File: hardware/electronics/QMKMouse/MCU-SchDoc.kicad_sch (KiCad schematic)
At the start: 14 parts

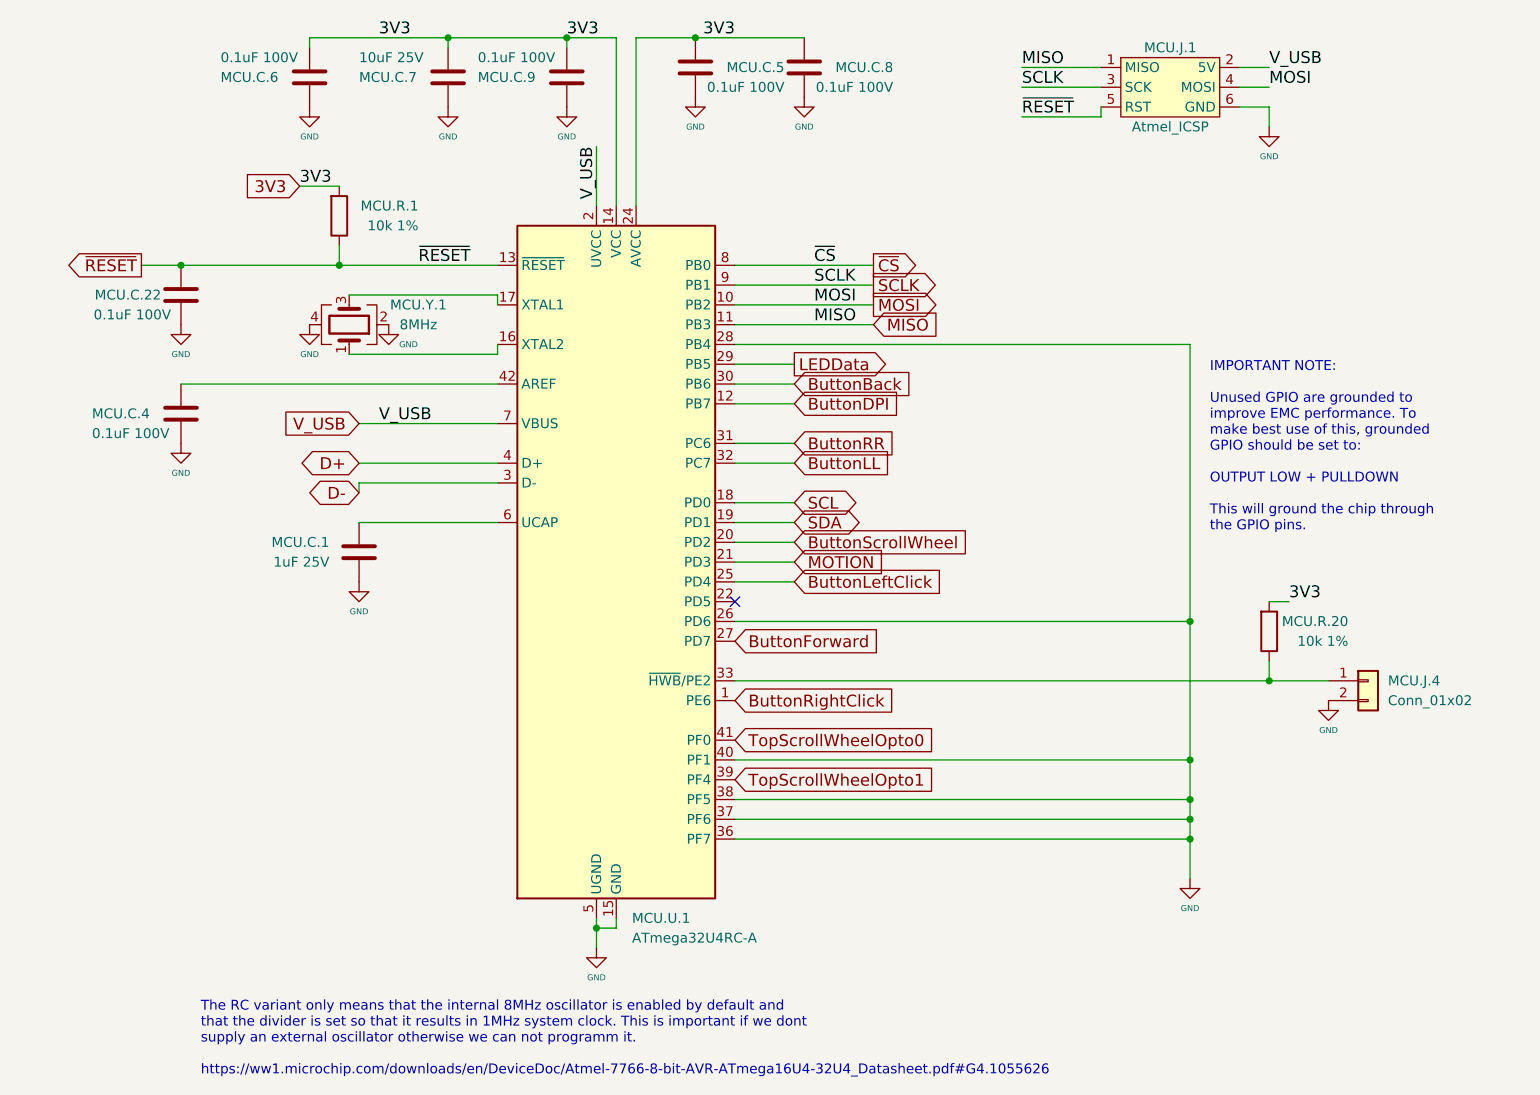
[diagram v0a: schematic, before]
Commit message: fix ERC errors and use hierarchy labels
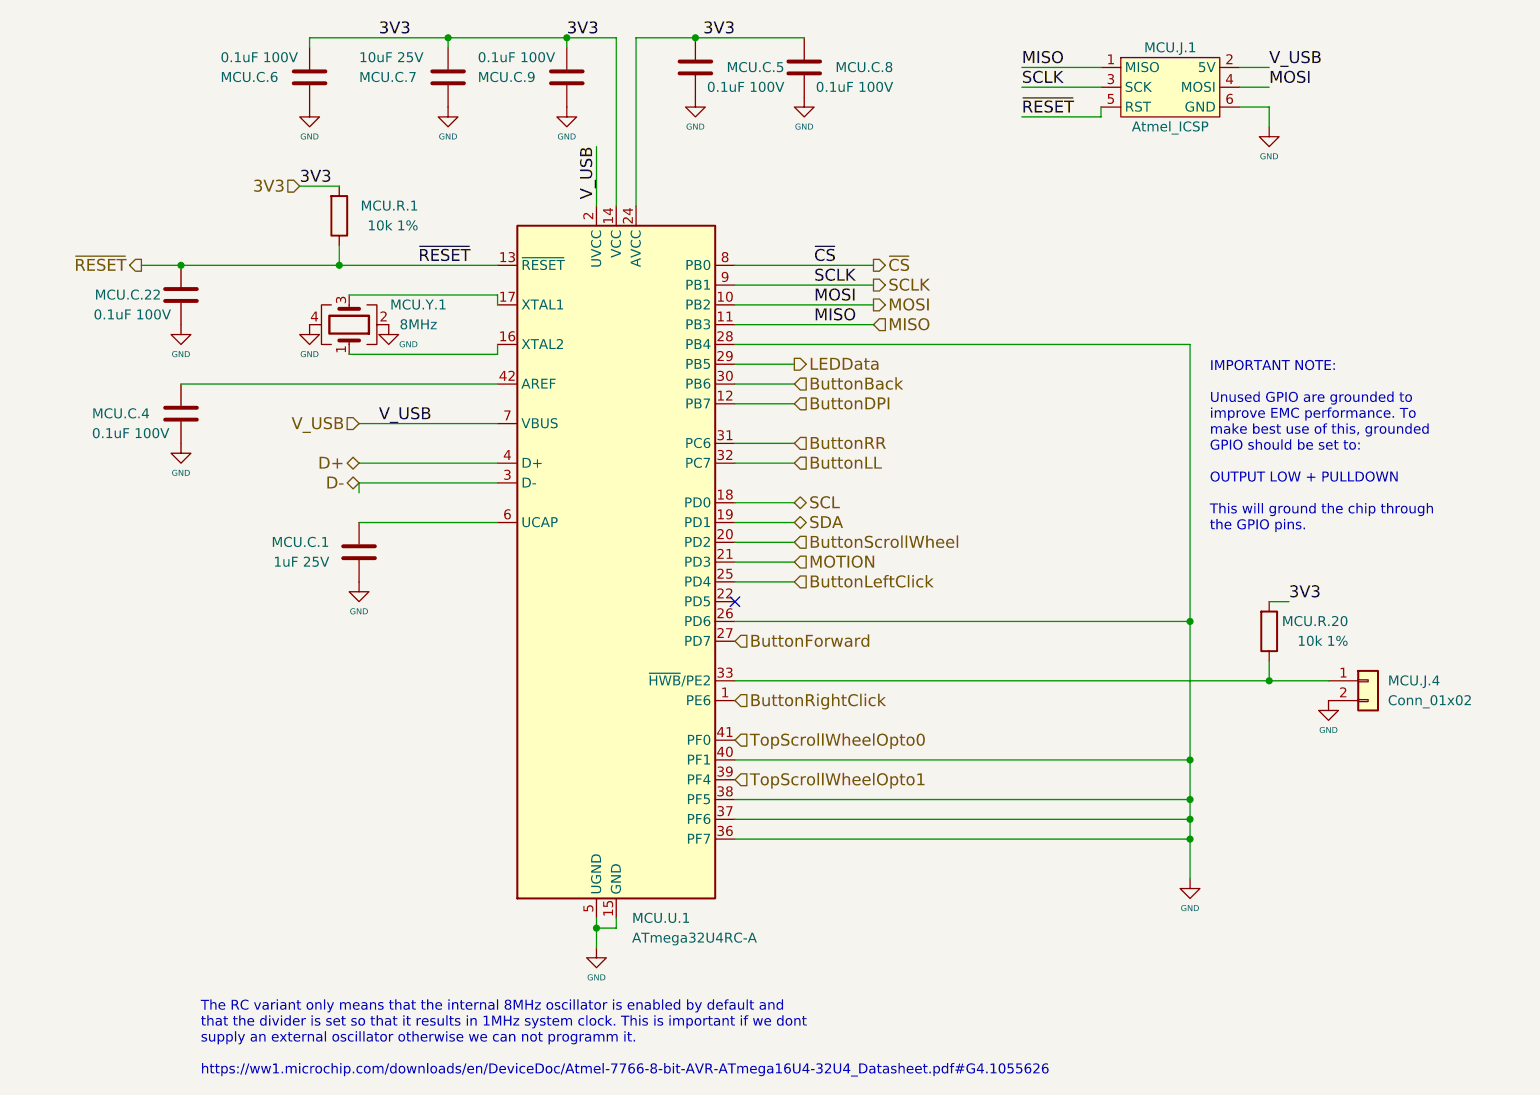
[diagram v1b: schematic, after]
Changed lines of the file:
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@@
     (effects (font (size 1.524 1.524)) (justify left bottom))
   )
-  (global_label "ButtonLeftClick" (shape input) (at 128.27 107.95 0) (fields_autoplaced)
+  (hierarchical_label "V_USB" (shape input) (at 72.39 87.63 180)
+    (effects (font (size 1.524 1.524)) (justify right))
+  )
+  (hierarchical_label "MOTION" (shape input) (at 128.27 105.41 0)
     (effects (font (size 1.524 1.524)) (justify left))
-    (property "Intersheet References" "${INTERSHEET_REFS}" (id 0) (at -90.17 -52.07 0)
-      (effects (font (size 1.27 1.27)) hide)
-    )
   )
-  (global_label "ButtonBack" (shape input) (at 128.27 82.55 0) (fields_autoplaced)
+  (hierarchical_label "~{CS}" (shape output) (at 138.43 67.31 0)
     (effects (font (size 1.524 1.524)) (justify left))
-    (property "Intersheet References" "${INTERSHEET_REFS}" (id 0) (at -90.17 -49.53 0)
-      (effects (font (size 1.27 1.27)) hide)
-    )
   )
-  (global_label "D+" (shape bidirectional) (at 72.39 92.71 180) (fields_autoplaced)
+  (hierarchical_label "MOSI" (shape output) (at 138.43 72.39 0)
+    (effects (font (size 1.524 1.524)) (justify left))
+  )
+  (hierarchical_label "ButtonRightClick" (shape input) (at 120.65 123.19 0)
+    (effects (font (size 1.524 1.524)) (justify left))
+  )
+  (hierarchical_label "SCL" (shape bidirectional) (at 128.27 97.79 0)
+    (effects (font (size 1.524 1.524)) (justify left))
+  )
+  (hierarchical_label "TopScrollWheelOpto0" (shape input) (at 120.65 128.27 0)
+    (effects (font (size 1.524 1.524)) (justify left))
+  )
+  (hierarchical_label "ButtonLL" (shape input) (at 128.27 92.71 0)
+    (effects (font (size 1.524 1.524)) (justify left))
+  )
+  (hierarchical_label "ButtonLeftClick" (shape input) (at 128.27 107.95 0)
+    (effects (font (size 1.524 1.524)) (justify left))
+  )
+  (hierarchical_label "3V3" (shape input) (at 64.77 57.15 180)
     (effects (font (size 1.524 1.524)) (justify right))
-    (property "Intersheet References" "${INTERSHEET_REFS}" (id 0) (at 166.37 217.17 0)
-      (effects (font (size 1.27 1.27)) (justify left) hide)
-    )
   )
-  (global_label "D-" (shape bidirectional) (at 72.39 96.52 180) (fields_autoplaced)
+  (hierarchical_label "ButtonRR" (shape input) (at 128.27 90.17 0)
+    (effects (font (size 1.524 1.524)) (justify left))
+  )
+  (hierarchical_label "ButtonForward" (shape input) (at 120.65 115.57 0)
+    (effects (font (size 1.524 1.524)) (justify left))
+  )
+  (hierarchical_label "ButtonBack" (shape input) (at 128.27 82.55 0)
+    (effects (font (size 1.524 1.524)) (justify left))
+  )
+  (hierarchical_label "SCLK" (shape output) (at 138.43 69.85 0)
+    (effects (font (size 1.524 1.524)) (justify left))
+  )
+  (hierarchical_label "ButtonDPI" (shape input) (at 128.27 85.09 0)
+    (effects (font (size 1.524 1.524)) (justify left))
+  )
+  (hierarchical_label "LEDData" (shape output) (at 128.27 80.01 0)
+    (effects (font (size 1.524 1.524)) (justify left))
+  )
+  (hierarchical_label "~{RESET}" (shape output) (at 44.45 67.31 180)
     (effects (font (size 1.524 1.524)) (justify right))
-    (property "Intersheet References" "${INTERSHEET_REFS}" (id 0) (at 166.37 215.9 0)
-      (effects (font (size 1.27 1.27)) (justify left) hide)
-    )
   )
-  (global_label "TopScrollWheelOpto1" (shape input) (at 120.65 133.35 0) (fields_autoplaced)
+  (hierarchical_label "TopScrollWheelOpto1" (shape input) (at 120.65 133.35 0)
     (effects (font (size 1.524 1.524)) (justify left))
-    (property "Intersheet References" "${INTERSHEET_REFS}" (id 0) (at -97.79 -52.07 0)
-      (effects (font (size 1.27 1.27)) hide)
-    )
   )
-  (global_label "~{CS}" (shape output) (at 138.43 67.31 0) (fields_autoplaced)
+  (hierarchical_label "D+" (shape bidirectional) (at 72.39 92.71 180)
+    (effects (font (size 1.524 1.524)) (justify right))
+  )
+  (hierarchical_label "MISO" (shape input) (at 138.43 74.93 0)
     (effects (font (size 1.524 1.524)) (justify left))
-    (property "Intersheet References" "${INTERSHEET_REFS}" (id 0) (at -97.79 -46.99 0)
-      (effects (font (size 1.27 1.27)) hide)
-    )
   )
-  (global_label "3V3" (shape input) (at 64.77 57.15 180) (fields_autoplaced)
+  (hierarchical_label "SDA" (shape bidirectional) (at 128.27 100.33 0)
+    (effects (font (size 1.524 1.524)) (justify left))
+  )
+  (hierarchical_label "ButtonScrollWheel" (shape input) (at 128.27 102.87 0)
+    (effects (font (size 1.524 1.524)) (justify left))
+  )
+  (hierarchical_label "D-" (shape bidirectional) (at 72.39 95.25 180)
     (effects (font (size 1.524 1.524)) (justify right))
-    (property "Intersheet References" "${INTERSHEET_REFS}" (id 0) (at 153.67 -97.79 0)
-      (effects (font (size 1.27 1.27)) (justify left) hide)
-    )
-  )
-  (global_label "ButtonRR" (shape input) (at 128.27 90.17 0) (fields_autoplaced)
-    (effects (font (size 1.524 1.524)) (justify left))
-    (property "Intersheet References" "${INTERSHEET_REFS}" (id 0) (at -90.17 -49.53 0)
-      (effects (font (size 1.27 1.27)) hide)
-    )
-  )
-  (global_label "ButtonScrollWheel" (shape input) (at 128.27 102.87 0) (fields_autoplaced)
-    (effects (font (size 1.524 1.524)) (justify left))
-    (property "Intersheet References" "${INTERSHEET_REFS}" (id 0) (at -90.17 -49.53 0)
-      (effects (font (size 1.27 1.27)) hide)
-    )
-  )
-  (global_label "TopScrollWheelOpto0" (shape input) (at 120.65 128.27 0) (fields_autoplaced)
-    (effects (font (size 1.524 1.524)) (justify left))
-    (property "Intersheet References" "${INTERSHEET_REFS}" (id 0) (at -97.79 -52.07 0)
-      (effects (font (size 1.27 1.27)) hide)
-    )
-  )
-  (global_label "ButtonRightClick" (shape input) (at 120.65 123.19 0) (fields_autoplaced)
-    (effects (font (size 1.524 1.524)) (justify left))
-    (property "Intersheet References" "${INTERSHEET_REFS}" (id 0) (at -97.79 -52.07 0)
-      (effects (font (size 1.27 1.27)) hide)
-    )
-  )
-  (global_label "LEDData" (shape output) (at 128.27 80.01 0) (fields_autoplaced)
-    (effects (font (size 1.524 1.524)) (justify left))
-    (property "Intersheet References" "${INTERSHEET_REFS}" (id 0) (at -90.17 -49.53 0)
-      (effects (font (size 1.27 1.27)) hide)
-    )
-  )
-  (global_label "MISO" (shape input) (at 138.43 74.93 0) (fields_autoplaced)
-    (effects (font (size 1.524 1.524)) (justify left))
-    (property "Intersheet References" "${INTERSHEET_REFS}" (id 0) (at -97.79 -46.99 0)
-      (effects (font (size 1.27 1.27)) hide)
-    )
-  )
-  (global_label "ButtonLL" (shape input) (at 128.27 92.71 0) (fields_autoplaced)
-    (effects (font (size 1.524 1.524)) (justify left))
-    (property "Intersheet References" "${INTERSHEET_REFS}" (id 0) (at -90.17 -49.53 0)
-      (effects (font (size 1.27 1.27)) hide)
-    )
-  )
-  (global_label "SCLK" (shape output) (at 138.43 69.85 0) (fields_autoplaced)
-    (effects (font (size 1.524 1.524)) (justify left))
-    (property "Intersheet References" "${INTERSHEET_REFS}" (id 0) (at -97.79 -46.99 0)
-      (effects (font (size 1.27 1.27)) hide)
-    )
-  )
-  (global_label "MOTION" (shape input) (at 128.27 105.41 0) (fields_autoplaced)
-    (effects (font (size 1.524 1.524)) (justify left))
-    (property "Intersheet References" "${INTERSHEET_REFS}" (id 0) (at -90.17 -49.53 0)
-      (effects (font (size 1.27 1.27)) hide)
-    )
-  )
-  (global_label "~{RESET}" (shape output) (at 44.45 67.31 180) (fields_autoplaced)
-    (effects (font (size 1.524 1.524)) (justify right))
-    (property "Intersheet References" "${INTERSHEET_REFS}" (id 0) (at 77.47 -97.79 0)
-      (effects (font (size 1.27 1.27)) (justify left) hide)
-    )
-  )
-  (global_label "MOSI" (shape output) (at 138.43 72.39 0) (fields_autoplaced)
-    (effects (font (size 1.524 1.524)) (justify left))
-    (property "Intersheet References" "${INTERSHEET_REFS}" (id 0) (at -97.79 -46.99 0)
-      (effects (font (size 1.27 1.27)) hide)
-    )
-  )
-  (global_label "V_USB" (shape input) (at 72.39 87.63 180) (fields_autoplaced)
-    (effects (font (size 1.524 1.524)) (justify right))
-    (property "Intersheet References" "${INTERSHEET_REFS}" (id 0) (at 166.37 -57.15 0)
-      (effects (font (size 1.27 1.27)) (justify left) hide)
-    )
-  )
-  (global_label "SDA" (shape bidirectional) (at 128.27 100.33 0) (fields_autoplaced)
-    (effects (font (size 1.524 1.524)) (justify left))
-    (property "Intersheet References" "${INTERSHEET_REFS}" (id 0) (at -90.17 -49.53 0)
-      (effects (font (size 1.27 1.27)) hide)
-    )
-  )
-  (global_label "SCL" (shape bidirectional) (at 128.27 97.79 0) (fields_autoplaced)
-    (effects (font (size 1.524 1.524)) (justify left))
-    (property "Intersheet References" "${INTERSHEET_REFS}" (id 0) (at -90.17 -49.53 0)
-      (effects (font (size 1.27 1.27)) hide)
-    )
-  )
-  (global_label "ButtonDPI" (shape input) (at 128.27 85.09 0) (fields_autoplaced)
-    (effects (font (size 1.524 1.524)) (justify left))
-    (property "Intersheet References" "${INTERSHEET_REFS}" (id 0) (at -90.17 -49.53 0)
-      (effects (font (size 1.27 1.27)) hide)
-    )
-  )
-  (global_label "ButtonForward" (shape input) (at 120.65 115.57 0) (fields_autoplaced)
-    (effects (font (size 1.524 1.524)) (justify left))
-    (property "Intersheet References" "${INTERSHEET_REFS}" (id 0) (at -97.79 -52.07 0)
-      (effects (font (size 1.27 1.27)) hide)
-    )
   )
   (symbol (lib_id "power:GND") (at 196.85 123.19 0) (unit 1)

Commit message: reference 3d model to all components
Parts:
- MCU.C.1, MCU.C.22, MCU.C.4, MCU.C.5, MCU.C.6, MCU.C.7, MCU.C.8, MCU.C.9: footprint Chip_Passives.PcbLib:0805 -> mouse_part:C_0805
- MCU.R.1, MCU.R.20: footprint Chip_Passives.PcbLib:0805 -> mouse_part:0805
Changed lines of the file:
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@@
       (effects (font (size 1.27 1.27)) (justify right))
     )
-    (property "Footprint" "Chip_Passives.PcbLib:0805" (id 2) (at 50.4952 67.31 0)
+    (property "Footprint" "mouse_part:C_0805" (id 2) (at 50.4952 67.31 0)
       (effects (font (size 1.27 1.27)) hide)
     )
@@
       (effects (font (size 1.27 1.27)) (justify left))
     )
-    (property "Footprint" "Chip_Passives.PcbLib:0805" (id 2) (at 50.4952 82.55 0)
+    (property "Footprint" "mouse_part:C_0805" (id 2) (at 50.4952 82.55 0)
       (effects (font (size 1.27 1.27)) hide)
     )
@@
       (effects (font (size 1.27 1.27)) (justify left))
     )
-    (property "Footprint" "Chip_Passives.PcbLib:0805" (id 2) (at 114.6048 38.1 0)
+    (property "Footprint" "mouse_part:C_0805" (id 2) (at 114.6048 38.1 0)
       (effects (font (size 1.27 1.27)) hide)
     )
@@
       (effects (font (size 1.27 1.27)) (justify left))
     )
-    (property "Footprint" "Chip_Passives.PcbLib:0805" (id 2) (at 100.0252 39.37 0)
+    (property "Footprint" "mouse_part:C_0805" (id 2) (at 100.0252 39.37 0)
       (effects (font (size 1.27 1.27)) hide)
     )
@@
       (effects (font (size 1.27 1.27)) (justify right))
     )
-    (property "Footprint" "Chip_Passives.PcbLib:0805" (id 2) (at 187.452 114.3 90)
+    (property "Footprint" "mouse_part:0805" (id 2) (at 187.452 114.3 90)
       (effects (font (size 1.27 1.27)) hide)
     )
@@
       (effects (font (size 1.27 1.27)) (justify right))
     )
-    (property "Footprint" "Chip_Passives.PcbLib:0805" (id 2) (at 68.072 60.96 90)
+    (property "Footprint" "mouse_part:0805" (id 2) (at 68.072 60.96 90)
       (effects (font (size 1.27 1.27)) hide)
     )
@@
       (effects (font (size 1.27 1.27)) (justify left))
     )
-    (property "Footprint" "Chip_Passives.PcbLib:0805" (id 2) (at 84.7852 39.37 0)
+    (property "Footprint" "mouse_part:C_0805" (id 2) (at 84.7852 39.37 0)
       (effects (font (size 1.27 1.27)) hide)
     )
@@
       (effects (font (size 1.27 1.27)) (justify left))
     )
-    (property "Footprint" "Chip_Passives.PcbLib:0805" (id 2) (at 67.0052 39.37 0)
+    (property "Footprint" "mouse_part:C_0805" (id 2) (at 67.0052 39.37 0)
       (effects (font (size 1.27 1.27)) hide)
     )
@@
       (effects (font (size 1.27 1.27)) (justify right))
     )
-    (property "Footprint" "Chip_Passives.PcbLib:0805" (id 2) (at 73.3552 100.33 0)
+    (property "Footprint" "mouse_part:C_0805" (id 2) (at 73.3552 100.33 0)
       (effects (font (size 1.27 1.27)) hide)
     )
@@
       (effects (font (size 1.27 1.27)) (justify right))
     )
-    (property "Footprint" "Chip_Passives.PcbLib:0805" (id 2) (at 130.5052 38.1 0)
-      (effects (font (size 1.27 1.27)) hide)
-    )
+    (property "Footprint" "mouse_part:C_0805" (id 2) (at 130.5052 38.1 0)
+      (effects (font (size 1.27 1.27)) hide)
+    )
